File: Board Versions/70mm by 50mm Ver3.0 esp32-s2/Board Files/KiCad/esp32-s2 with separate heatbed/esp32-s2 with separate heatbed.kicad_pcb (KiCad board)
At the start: 2 copper layers, 125.7 x 83.8 mm, 60 parts, among them IC1 ESP32-S2FN4R2, J1 PJ-037B, J2 USB4520-03-0-A, J3 TB003-500-P02BE, J4 TB003-500-P02BE, Q1 PJD25N06A_L2_00001, U1 LD1117S33TR_SOT223, U2 MAX31855KASA, Y1 ECS-400-15-33B-CTN-TR

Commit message: Routing complete
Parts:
- removed the REF** at (20.3, 20.3)
- removed TP1, TP2, TP3, TP4, TP5, TP6: TestPoint, Connector_PinHeader_2.54mm:PinHeader_1x01_P2.54mm_Vertical
- added J5: Conn_01x03_Male, Connector_PinHeader_2.54mm:PinHeader_1x03_P2.54mm_Vertical, F.Cu at (75.1, 34.8)
- added REF**: -, MountingHole:MountingHole_3.2mm_M3_Pad_Via, F.Cu at (20.0, 20.0)
- added REF**: -, MountingHole:MountingHole_3.2mm_M3_Pad_Via, F.Cu at (74.0, 20.0)
- added REF**: -, MountingHole:MountingHole_3.2mm_M3_Pad_Via, F.Cu at (74.0, 57.0)
- added REF**: -, MountingHole:MountingHole_3.2mm_M3_Pad_Via, F.Cu at (20.0, 57.0)
- moved C8 202.5 mm to (58.9, 28.1), turned to 90 degrees
- moved U2 199.0 mm to (63.8, 27.1)
- moved J4 192.4 mm to (61.1, 19.6)
- moved C22 159.0 mm to (62.5, 43.4), turned to -90 degrees
- moved R8 158.0 mm to (30.1, 54.5), turned to 180 degrees
- moved S2 157.0 mm to (67.3, 48.4)
- moved R3 157.0 mm to (60.5, 43.5), turned to 90 degrees
- moved R7 155.9 mm to (26.0, 59.0), turned to 180 degrees
- moved R5 155.1 mm to (62.6, 48.3), turned to -90 degrees
- moved S1 154.7 mm to (67.3, 43.3)
- moved ANT1 152.7 mm to (30.1, 59.0)
- moved D3 147.1 mm to (65.8, 37.6), turned to 180 degrees
- moved R11 145.9 mm to (65.8, 35.3), turned to 180 degrees
- moved C9 143.7 mm to (49.0, 45.7), turned to -90 degrees
- moved D6 143.7 mm to (65.8, 33.4), turned to 180 degrees
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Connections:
- IC1 pad 16: Net-(IC1-Pad16) -> unconnected-(IC1-Pad16)
- IC1 pad 17: Net-(IC1-Pad17) -> unconnected-(IC1-Pad17)
- IC1 pad 23: Net-(IC1-Pad23) -> unconnected-(IC1-Pad23)
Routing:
- net +3V3: track 0.00 -> 147.2 mm, vias 0 -> 2
- net EN: track 0.00 -> 64.6 mm, vias 0 -> 2
- net D+: track 3.02 -> 62.0 mm, vias 0 -> 2
- net led2: track 0.00 -> 58.2 mm, vias 0 -> 2
- net D-: track 2.99 -> 61.0 mm, vias 0 -> 2
- net led1: track 0.00 -> 55.1 mm, vias 0 -> 2
- net FLASH: track 0.00 -> 55.0 mm, vias 0 -> 2
- net tempSO: track 0.00 -> 42.0 mm, vias 0 -> 2
- net Net-(IC1-Pad37): track 0.00 -> 39.0 mm, vias 0 -> 1
- net tempCS: track 0.00 -> 38.5 mm, vias 0 -> 2
- net tempSCK: track 0.00 -> 38.3 mm, vias 0 -> 2
- net Net-(IC1-Pad38): track 0.00 -> 38.1 mm, vias 0 -> 1
- net Net-(IC1-Pad39): track 0.00 -> 38.0 mm, vias 0 -> 1
- net heatGate: track 4.24 -> 40.1 mm, vias 0 -> 2
- net XTAL_N: track 0.00 -> 22.2 mm, vias 0 -> 2
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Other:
- board size 125.7 x 83.8 mm -> 65.5 x 50 mm
- board text added: "BOOT"
- board text added: "RST"
- board text added: "Reflow esp32-32 v1"

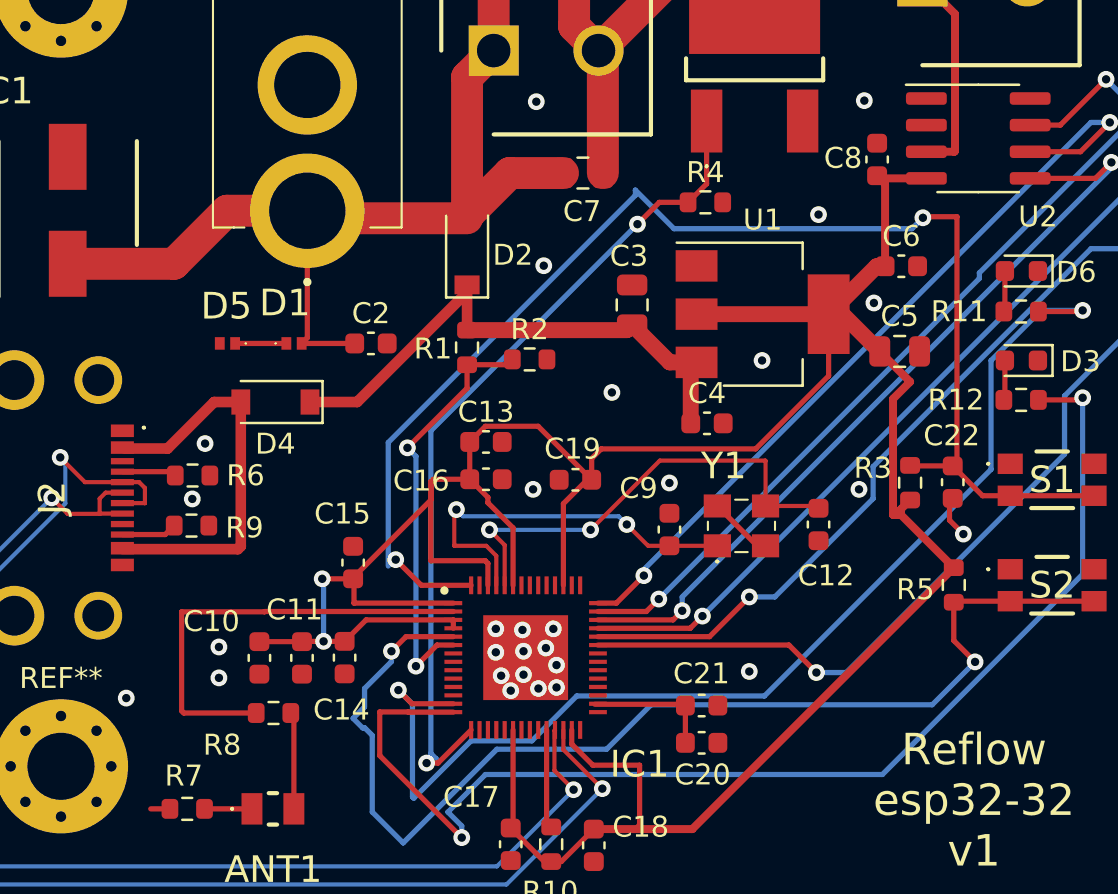
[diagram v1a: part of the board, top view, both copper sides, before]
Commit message: Add C for antenna
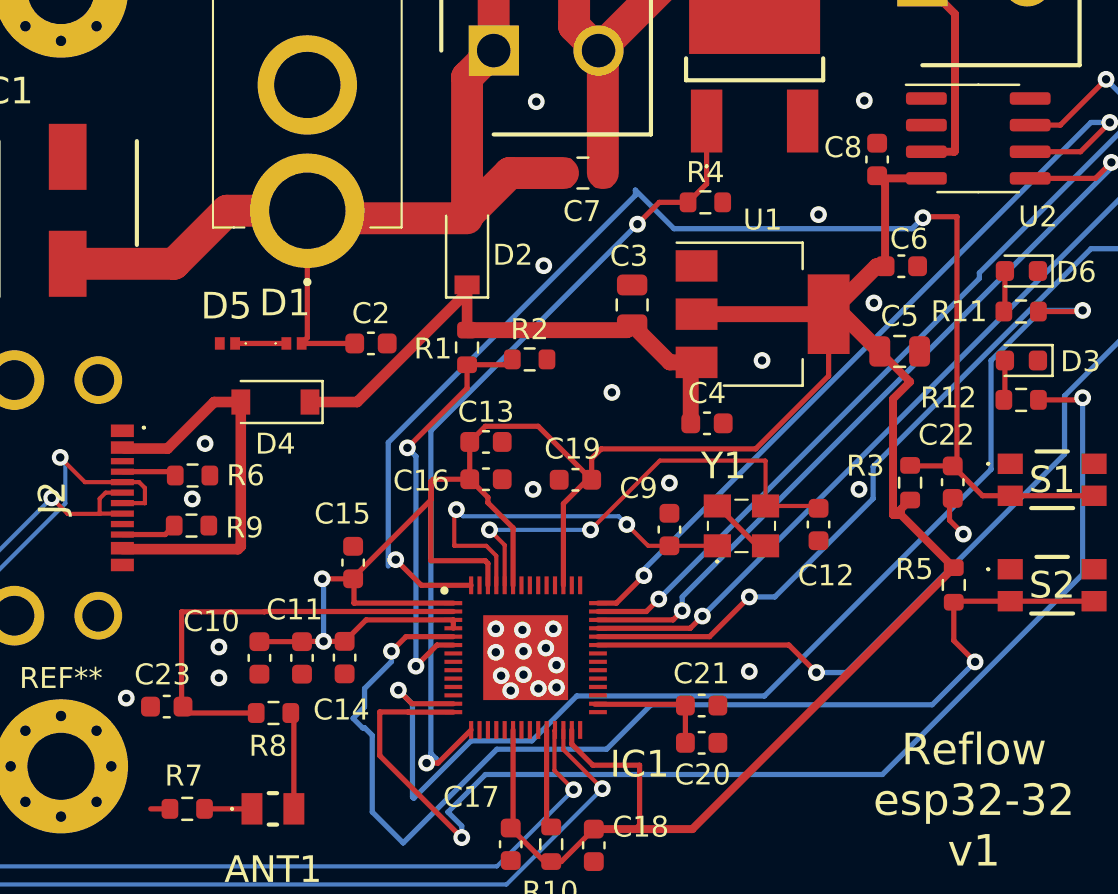
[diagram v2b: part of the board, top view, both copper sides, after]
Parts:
- added C23: ?, Capacitor_SMD:C_0603_1608Metric, F.Cu at (25.0, 54.2)
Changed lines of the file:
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@@
     (property "Sheetname" "")
     (attr smd)
-    (fp_text reference "R8" (at 2.4506 -1.524) (layer "F.SilkS")
+    (fp_text reference "R8" (at 0.2662 -1.5748) (layer "F.SilkS")
       (effects (font (size 1 1) (thickness 0.15)))
     )
@@
     (property "Sheetname" "")
     (attr smd)
-    (fp_text reference "R5" (at 0.2154 1.8288 180) (layer "F.SilkS")
+    (fp_text reference "R5" (at -0.7498 1.8796 180) (layer "F.SilkS")
       (effects (font (size 1 1) (thickness 0.15)))
     )
@@
     (property "Sheetname" "")
     (attr smd)
-    (fp_text reference "R3" (at 0.699 -1.778) (layer "F.SilkS")
+    (fp_text reference "R3" (at 0.8006 -2.1336) (layer "F.SilkS")
       (effects (font (size 1 1) (thickness 0.15)))
     )
@@
     (property "Sheetname" "")
     (attr smd)
-    (fp_text reference "R12" (at 3.111 0) (layer "F.SilkS")
+    (fp_text reference "R12" (at 3.4666 0.1016) (layer "F.SilkS")
       (effects (font (size 1 1) (thickness 0.15)))
     )
@@
     (property "Sheetname" "")
     (attr smd)
-    (fp_text reference "C8" (at 0.0632 -1.6256 180) (layer "F.SilkS")
+    (fp_text reference "C8" (at 0.5712 -1.6256 180) (layer "F.SilkS")
       (effects (font (size 1 1) (thickness 0.15)))
     )
@@
     (property "Sheetname" "")
     (attr smd)
-    (fp_text reference "C22" (at -2.2222 0.0508) (layer "F.SilkS")
+    (fp_text reference "C22" (at -2.2482 0.3048) (layer "F.SilkS")
       (effects (font (size 1 1) (thickness 0.15)))
     )
@@
   )
   (footprint "Capacitor_SMD:C_0603_1608Metric" (layer "F.Cu")
+    (at 25.0444 54.1528 180)
+    (descr "Capacitor SMD 0603 (1608 Metric), square (rectangular) end terminal, IPC_7351 nominal, (Body size source: IPC-SM-782 page 76, https://www.pcb-3d.com/wordpress/wp-content/uploads/ipc-sm-782a_amendment_1_and_2.pdf), generated with kicad-footprint-generator")
+    (tags "capacitor")
+    (property "Sheetfile" "esp32-s2 with separate heatbed.kicad_sch")
+    (property "Sheetname" "")
+    (attr smd)
+    (fp_text reference "C23" (at 0.2032 1.524) (layer "F.SilkS")
+      (effects (font (size 1 1) (thickness 0.15)))
+    )
+    (fp_text value "?" (at 0 1.43) (layer "F.Fab")
+      (effects (font (size 1 1) (thickness 0.15)))
+    )
+    (fp_text user "${REFERENCE}" (at 0 0) (layer "F.Fab")
+      (effects (font (size 0.4 0.4) (thickness 0.06)))
+    )
+    (fp_line (start -0.14058 0.51) (end 0.14058 0.51) (layer "F.SilkS") (width 0.12))
+    (fp_line (start -0.14058 -0.51) (end 0.14058 -0.51) (layer "F.SilkS") (width 0.12))
+    (fp_line (start -1.48 0.73) (end -1.48 -0.73) (layer "F.CrtYd") (width 0.05))
+    (fp_line (start -1.48 -0.73) (end 1.48 -0.73) (layer "F.CrtYd") (width 0.05))
+    (fp_line (start 1.48 -0.73) (end 1.48 0.73) (layer "F.CrtYd") (width 0.05))
+    (fp_line (start 1.48 0.73) (end -1.48 0.73) (layer "F.CrtYd") (width 0.05))
+    (fp_line (start 0.8 -0.4) (end 0.8 0.4) (layer "F.Fab") (width 0.1))
+    (fp_line (start -0.8 0.4) (end -0.8 -0.4) (layer "F.Fab") (width 0.1))
+    (fp_line (start 0.8 0.4) (end -0.8 0.4) (layer "F.Fab") (width 0.1))
+    (fp_line (start -0.8 -0.4) (end 0.8 -0.4) (layer "F.Fab") (width 0.1))
+    (pad "1" smd roundrect (at -0.775 0 180) (size 0.9 0.95) (layers "F.Cu" "F.Paste" "F.Mask") (roundrect_rratio 0.25)
+      (net 16 "ANT") (pintype "passive"))
+    (pad "2" smd roundrect (at 0.775 0 180) (size 0.9 0.95) (layers "F.Cu" "F.Paste" "F.Mask") (roundrect_rratio 0.25)
+      (net 4 "GND") (pintype "passive"))
+    (model "${KICAD6_3DMODEL_DIR}/Capacitor_SMD.3dshapes/C_0603_1608Metric.wrl"
+      (offset (xyz 0 0 0))
+      (scale (xyz 1 1 1))
+      (rotate (xyz 0 0 0))
+    )
+  )
+  (footprint "Capacitor_SMD:C_0603_1608Metric" (layer "F.Cu")
     (at 60.084 33.147)
     (descr "Capacitor SMD 0603 (1608 Metric), square (rectangular) end terminal, IPC_7351 nominal, (Body size source: IPC-SM-782 page 76, https://www.pcb-3d.com/wordpress/wp-content/uploads/ipc-sm-782a_amendment_1_and_2.pdf), generated with kicad-footprint-generator")
@@
     (property "Sheetname" "")
     (attr smd)
-    (fp_text reference "C6" (at 0 -1.43) (layer "F.SilkS")
-      (effects (font (size 1 1) (thickness 0.15)))
-    )
+    (fp_text reference "C6" (at 0.368 -1.2954) (layer "F.SilkS")
+      (effects (font (size 1 1) (thickness 0.15)))
+    )
